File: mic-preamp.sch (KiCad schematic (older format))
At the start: 29 parts, among them P1 CONN_4, U1 MCP6234-E/SL, U2 LM339

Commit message: Started working on pcb
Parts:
- R2: value 4.7k -> 470
- R3: value 4.7k -> 6.8k
- R4: value 4.7k -> 3.9k
- R5: value 4.7k -> 1.8k
- R6: value 4.7k -> 15k
- R7: value 4.7k -> 2.2k
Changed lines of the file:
@@
 LIBS:valves
 LIBS:visgence_parts
+LIBS:mic-preamp-cache
 EELAYER 24 0
 EELAYER END
@@
 P 3200 2900
 F 0 "R7" V 3280 2900 40  0000 C CNN
-F 1 "4.7k" V 3207 2901 40  0000 C CNN
+F 1 "2.2k" V 3207 2901 40  0000 C CNN
 F 2 "" V 3130 2900 30  0000 C CNN
 F 3 "" H 3200 2900 30  0000 C CNN
@@
 P 3150 7200
 F 0 "R6" V 3230 7200 40  0000 C CNN
-F 1 "4.7k" V 3157 7201 40  0000 C CNN
+F 1 "15k" V 3157 7201 40  0000 C CNN
 F 2 "" V 3080 7200 30  0000 C CNN
 F 3 "" H 3150 7200 30  0000 C CNN
@@
 P 3150 6400
 F 0 "R5" V 3230 6400 40  0000 C CNN
-F 1 "4.7k" V 3157 6401 40  0000 C CNN
+F 1 "1.8k" V 3157 6401 40  0000 C CNN
 F 2 "" V 3080 6400 30  0000 C CNN
 F 3 "" H 3150 6400 30  0000 C CNN
@@
 P 3150 5700
 F 0 "R4" V 3230 5700 40  0000 C CNN
-F 1 "4.7k" V 3157 5701 40  0000 C CNN
+F 1 "3.9k" V 3157 5701 40  0000 C CNN
 F 2 "" V 3080 5700 30  0000 C CNN
 F 3 "" H 3150 5700 30  0000 C CNN
@@
 P 3150 4900
 F 0 "R3" V 3230 4900 40  0000 C CNN
-F 1 "4.7k" V 3157 4901 40  0000 C CNN
+F 1 "6.8k" V 3157 4901 40  0000 C CNN
 F 2 "" V 3080 4900 30  0000 C CNN
 F 3 "" H 3150 4900 30  0000 C CNN
@@
 P 3150 4250
 F 0 "R2" V 3230 4250 40  0000 C CNN
-F 1 "4.7k" V 3157 4251 40  0000 C CNN
+F 1 "470" V 3157 4251 40  0000 C CNN
 F 2 "" V 3080 4250 30  0000 C CNN
 F 3 "" H 3150 4250 30  0000 C CNN

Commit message: Routed and generated gerber
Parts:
- added C4: 47u, symbol C
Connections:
- net +5V: now also P1.3 (P3), C4.2; no longer P1.2 (P2)
- net GND: now also P1.4 (P4), C4.1; no longer P1.1 (P1)
- net out: now also P1.1 (P1); no longer P1.4 (P4)
- no-connect marks 0 -> 2
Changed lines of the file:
@@
 $EndComp
 $Comp
-L GND #PWR01
+L GND #PWR5
 U 1 1 53E1A238
 P 3150 3550
-F 0 "#PWR01" H 3150 3550 30  0001 C CNN
+F 0 "#PWR5" H 3150 3550 30  0001 C CNN
 F 1 "GND" H 3150 3480 30  0001 C CNN
 F 2 "" H 3150 3550 60  0000 C CNN
@@
 $EndComp
 $Comp
-L +5V #PWR02
+L +5V #PWR8
 U 1 1 53E1A750
 P 3200 2500
-F 0 "#PWR02" H 3200 2590 20  0001 C CNN
+F 0 "#PWR8" H 3200 2590 20  0001 C CNN
 F 1 "+5V" H 3200 2590 30  0000 C CNN
 F 2 "" H 3200 2500 60  0000 C CNN
@@
 $EndComp
 $Comp
-L GND #PWR03
+L GND #PWR10
 U 1 1 53E1AA8C
 P 3750 2450
-F 0 "#PWR03" H 3750 2450 30  0001 C CNN
+F 0 "#PWR10" H 3750 2450 30  0001 C CNN
 F 1 "GND" H 3750 2380 30  0001 C CNN
 F 2 "" H 3750 2450 60  0000 C CNN
@@
 $EndComp
 $Comp
-L +5V #PWR04
+L +5V #PWR9
 U 1 1 53E1AC33
 P 3750 950
-F 0 "#PWR04" H 3750 1040 20  0001 C CNN
+F 0 "#PWR9" H 3750 1040 20  0001 C CNN
 F 1 "+5V" H 3750 1040 30  0000 C CNN
 F 2 "" H 3750 950 60  0000 C CNN
@@
 $EndComp
 $Comp
-L +5V #PWR05
+L +5V #PWR6
 U 1 1 53E1CF4F
 P 3150 3900
-F 0 "#PWR05" H 3150 3990 20  0001 C CNN
+F 0 "#PWR6" H 3150 3990 20  0001 C CNN
 F 1 "+5V" H 3150 3990 30  0000 C CNN
 F 2 "" H 3150 3900 60  0000 C CNN
@@
 Connection ~ 5950 6250
 $Comp
-L +5V #PWR06
+L +5V #PWR15
 U 1 1 53E1F75C
 P 5950 4450
-F 0 "#PWR06" H 5950 4540 20  0001 C CNN
+F 0 "#PWR15" H 5950 4540 20  0001 C CNN
 F 1 "+5V" H 5950 4540 30  0000 C CNN
 F 2 "" H 5950 4450 60  0000 C CNN
@@
 Connection ~ 5950 4750
 $Comp
-L GND #PWR07
+L GND #PWR7
 U 1 1 53E1F9B9
 P 3150 7600
-F 0 "#PWR07" H 3150 7600 30  0001 C CNN
+F 0 "#PWR7" H 3150 7600 30  0001 C CNN
 F 1 "GND" H 3150 7530 30  0001 C CNN
 F 2 "" H 3150 7600 60  0000 C CNN
@@
 	3150 7450 3150 7600
 $Comp
-L GND #PWR08
+L GND #PWR14
 U 1 1 53E1FBF6
 P 4500 2350
-F 0 "#PWR08" H 4500 2350 30  0001 C CNN
+F 0 "#PWR14" H 4500 2350 30  0001 C CNN
 F 1 "GND" H 4500 2280 30  0001 C CNN
 F 2 "" H 4500 2350 60  0000 C CNN
@@
 $EndComp
 $Comp
-L +5V #PWR09
+L +5V #PWR13
 U 1 1 53E1FDA1
 P 4500 1250
-F 0 "#PWR09" H 4500 1340 20  0001 C CNN
+F 0 "#PWR13" H 4500 1340 20  0001 C CNN
 F 1 "+5V" H 4500 1340 30  0000 C CNN
 F 2 "" H 4500 1250 60  0000 C CNN
@@
 $EndComp
 $Comp
-L +5V #PWR010
+L +5V #PWR16
 U 1 1 53E226A8
-P 7850 4650
-F 0 "#PWR010" H 7850 4740 20  0001 C CNN
-F 1 "+5V" H 7850 4740 30  0000 C CNN
-F 2 "" H 7850 4650 60  0000 C CNN
-F 3 "" H 7850 4650 60  0000 C CNN
-	1    7850 4650
-	1    0    0    -1
-$EndComp
-$Comp
-L GND #PWR011
+P 7950 4650
+F 0 "#PWR16" H 7950 4740 20  0001 C CNN
+F 1 "+5V" H 7950 4740 30  0000 C CNN
+F 2 "" H 7950 4650 60  0000 C CNN
+F 3 "" H 7950 4650 60  0000 C CNN
+	1    7950 4650
+	1    0    0    -1
+$EndComp
+$Comp
+L GND #PWR17
 U 1 1 53E229B4
-P 7550 4900
-F 0 "#PWR011" H 7550 4900 30  0001 C CNN
-F 1 "GND" H 7550 4830 30  0001 C CNN
-F 2 "" H 7550 4900 60  0000 C CNN
-F 3 "" H 7550 4900 60  0000 C CNN
-	1    7550 4900
-	1    0    0    -1
-$EndComp
-Wire Wire Line
-	7550 4900 7550 4700
-Wire Wire Line
-	7550 4700 7750 4700
+P 8300 4850
+F 0 "#PWR17" H 8300 4850 30  0001 C CNN
+F 1 "GND" H 8300 4780 30  0001 C CNN
+F 2 "" H 8300 4850 60  0000 C CNN
+F 3 "" H 8300 4850 60  0000 C CNN
+	1    8300 4850
+	1    0    0    -1
+$EndComp
 Wire Wire Line
 	7750 4700 7750 4800
-Wire Wire Line
-	7850 4650 7850 4800
-Text GLabel 8050 4600 1    39   Input ~ 0
+Text GLabel 7750 4700 1    39   Input ~ 0
 out
 Wire Wire Line
@@
 $EndComp
 $Comp
-L +5V #PWR012
+L +5V #PWR3
 U 1 1 53E23B2D
 P 2300 950
-F 0 "#PWR012" H 2300 1040 20  0001 C CNN
+F 0 "#PWR3" H 2300 1040 20  0001 C CNN
 F 1 "+5V" H 2300 1040 30  0000 C CNN
 F 2 "" H 2300 950 60  0000 C CNN
@@
 	2300 1600 2300 1750
 $Comp
-L GND #PWR013
+L GND #PWR4
 U 1 1 53E23D4F
 P 2300 2350
-F 0 "#PWR013" H 2300 2350 30  0001 C CNN
+F 0 "#PWR4" H 2300 2350 30  0001 C CNN
 F 1 "GND" H 2300 2280 30  0001 C CNN
 F 2 "" H 2300 2350 60  0000 C CNN
@@
 	2300 2150 2300 2350
 $Comp
-L +5V #PWR014
+L +5V #PWR11
 U 1 1 53E25F5C
 P 3850 4350
-F 0 "#PWR014" H 3850 4440 20  0001 C CNN
+F 0 "#PWR11" H 3850 4440 20  0001 C CNN
 F 1 "+5V" H 3850 4440 30  0000 C CNN
 F 2 "" H 3850 4350 60  0000 C CNN
@@
 	3850 4350 3850 4450
 $Comp
-L GND #PWR015
+L GND #PWR12
 U 1 1 53E26219
 P 3850 7550
-F 0 "#PWR015" H 3850 7550 30  0001 C CNN
+F 0 "#PWR12" H 3850 7550 30  0001 C CNN
 F 1 "GND" H 3850 7480 30  0001 C CNN
 F 2 "" H 3850 7550 60  0000 C CNN
@@
 Wire Wire Line
 	3850 7350 3850 7550
+Wire Wire Line
+	8050 4600 8300 4600
+Wire Wire Line
+	8300 4600 8300 4850
+Wire Wire Line
+	7950 4650 7950 4800
+NoConn ~ 7850 4800
+NoConn ~ 7100 3750
+$Comp
+L C C4
+U 1 1 53E30428
+P 1700 1600
+F 0 "C4" H 1700 1700 40  0000 L CNN
+F 1 "47u" H 1706 1515 40  0000 L CNN
+F 2 "" H 1738 1450 30  0000 C CNN
+F 3 "" H 1700 1600 60  0000 C CNN
+	1    1700 1600
+	-1   0    0    1
+$EndComp
+$Comp
+L +5V #PWR1
+U 1 1 53E30598
+P 1700 1100
+F 0 "#PWR1" H 1700 1190 20  0001 C CNN
+F 1 "+5V" H 1700 1190 30  0000 C CNN
+F 2 "" H 1700 1100 60  0000 C CNN
+F 3 "" H 1700 1100 60  0000 C CNN
+	1    1700 1100
+	1    0    0    -1
+$EndComp
+Wire Wire Line
+	1700 1100 1700 1400
+$Comp
+L GND #PWR2
+U 1 1 53E306A0
+P 1700 1950
+F 0 "#PWR2" H 1700 1950 30  0001 C CNN
+F 1 "GND" H 1700 1880 30  0001 C CNN
+F 2 "" H 1700 1950 60  0000 C CNN
+F 3 "" H 1700 1950 60  0000 C CNN
+	1    1700 1950
+	1    0    0    -1
+$EndComp
+Wire Wire Line
+	1700 1800 1700 1950
 $EndSCHEMATC

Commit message: Fixed solder mask
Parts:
- C1, C2, C3: footprint (none) -> visgence_parts:SM0603_Capa_VIS
- C4: footprint (none) -> visgence_parts:SM1206POL_VIS
- D1, D2, D3, D4, D5: footprint (none) -> LEDs:LED-0603
- MIC1: footprint (none) -> visgence_parts:MIC9.7
- P1: footprint (none) -> Connect:bornier4
- R1, R10, R11, R12, R13, R14, R15, R16, R2, R3, R4, R5, R6, R7, R8, R9: footprint (none) -> visgence_parts:SM0603_VIS
- RV1: footprint (none) -> visgence_parts:TC33X-2
- U1, U2: footprint (none) -> SMD_Packages:SO14E

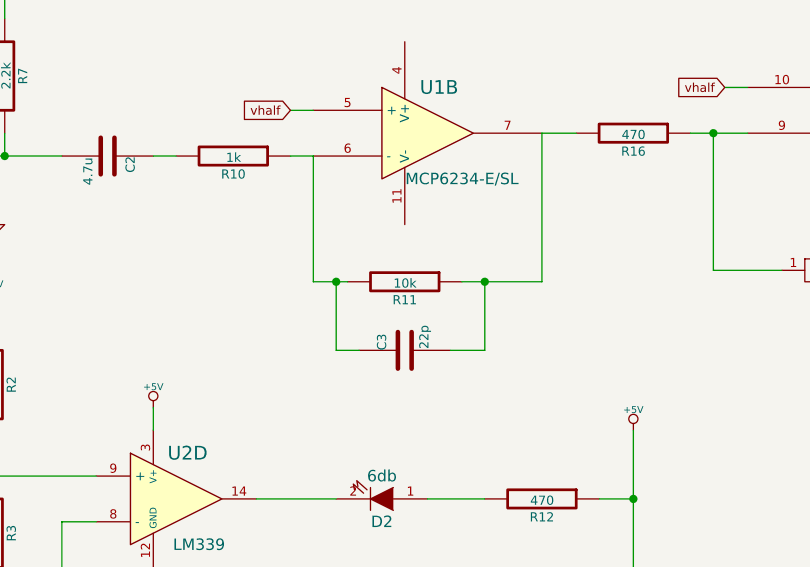
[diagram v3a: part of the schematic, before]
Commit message: resized board, change gain
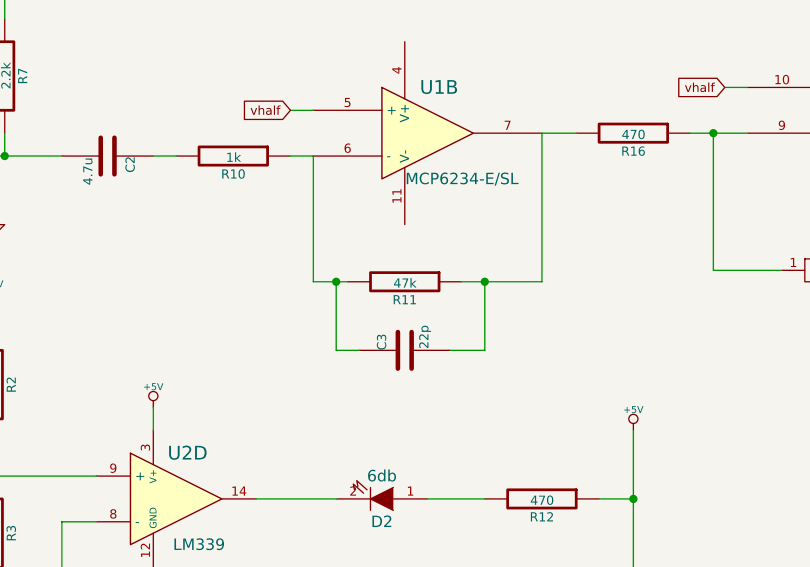
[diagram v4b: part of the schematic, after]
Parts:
- R11: value 10k -> 47k
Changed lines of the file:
@@
 P 4950 3800
 F 0 "R11" V 5030 3800 40  0000 C CNN
-F 1 "10k" V 4957 3801 40  0000 C CNN
+F 1 "47k" V 4957 3801 40  0000 C CNN
 F 2 "visgence_parts:SM0603_VIS" V 4880 3800 30  0001 C CNN
 F 3 "" H 4950 3800 30  0000 C CNN
